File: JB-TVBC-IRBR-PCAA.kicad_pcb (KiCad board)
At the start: 2 copper layers, 20 x 25 mm, 7 parts, among them J1 SJ-435107, U1 TSOP75338WTT

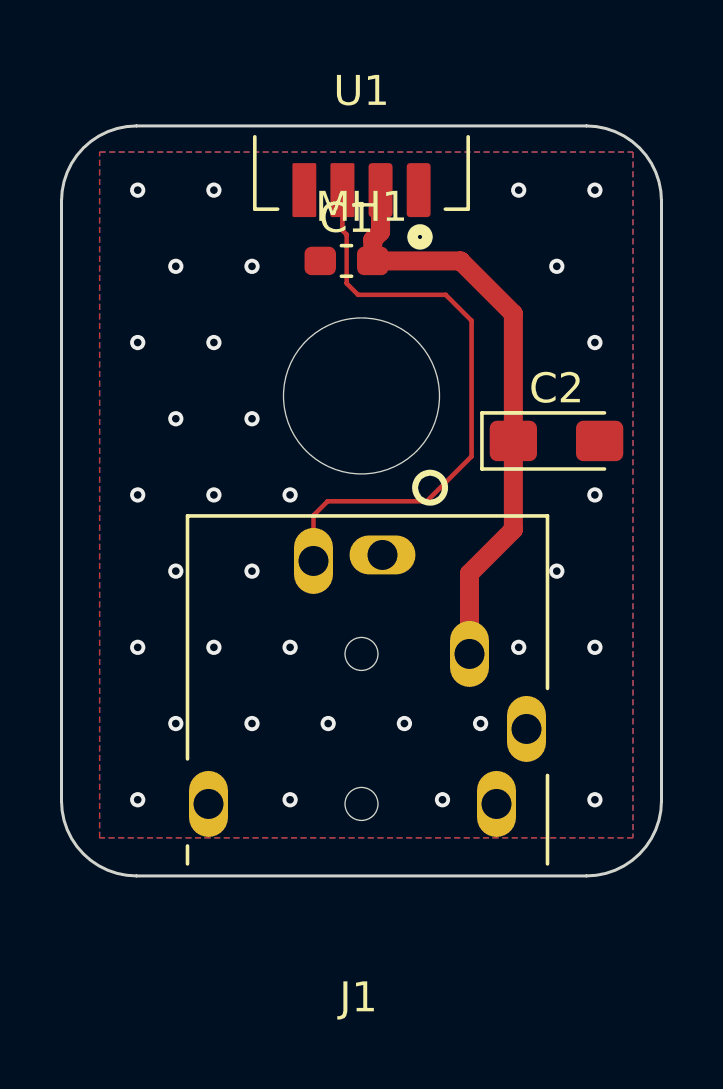
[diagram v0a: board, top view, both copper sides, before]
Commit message: clearing case + ref designator positioning
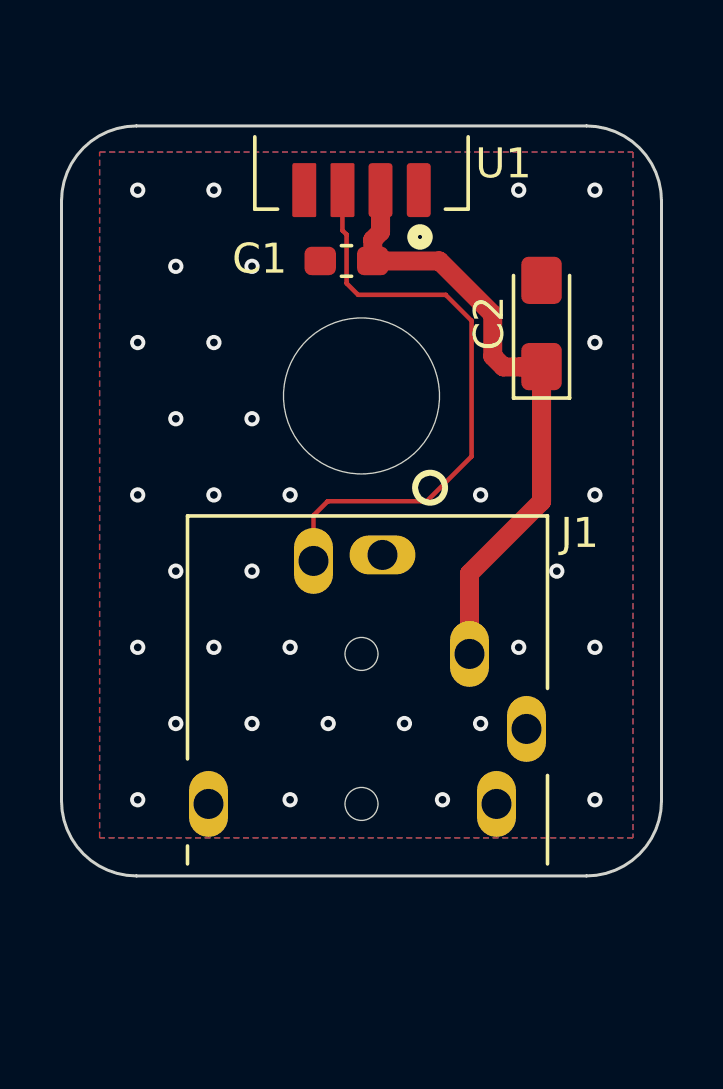
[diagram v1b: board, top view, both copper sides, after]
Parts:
- moved C2 3.95 mm to (156.0, 161.6), turned to 90 degrees
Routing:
- net +3V3: track 19.8 -> 21.0 mm
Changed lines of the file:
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@@
     (thickness 1.6)
     (drawings 11)
-    (tracks 53)
+    (tracks 57)
     (zones 0)
     (modules 7)
@@
   )
   (setup
-    (last_trace_width 0.1524)
+    (last_trace_width 0.635)
     (user_trace_width 0.1524)
     (user_trace_width 0.254)
@@
     (descr "TRS 3.5mm, horizontal, through-hole, with switch, circular holes, https://www.cui.com/product/resource/sj1-353xng.pdf")
     (tags "TRS audio jack stereo horizontal circular")
-    (fp_text reference J1 (at 0.1 -6.45 180) (layer F.SilkS)
+    (fp_text reference J1 (at -7.272 9.03 180) (layer F.SilkS)
       (effects (font (size 1 1) (thickness 0.15)))
     )
@@
     (tags "through hole")
     (attr virtual)
-    (fp_text reference MH1 (at 0 -6.3) (layer F.SilkS)
+    (fp_text reference MH1 (at 0 -6.3) (layer F.SilkS) hide
       (effects (font (size 1 1) (thickness 0.15)))
     )
@@
     (descr "TSOP753xx Right Angle")
     (tags "ir, ir receiver")
-    (fp_text reference U1 (at 0 2.413) (layer F.SilkS)
+    (fp_text reference U1 (at -4.732 -0.001) (layer F.SilkS)
       (effects (font (size 1 1) (thickness 0.15)))
     )
@@
   )
   (module Capacitor_Tantalum_SMD:CP_EIA-3216-18_Kemet-A_Pad1.58x1.35mm_HandSolder (layer F.Cu)
-    (at 156.5 165.5)
+    (at 156.002 161.585 90)
     (descr "Tantalum Capacitor SMD Kemet-A (3216-18 Metric), IPC_7351 nominal, (Body size from: http://www.kemet.com/Lists/ProductCatalog/Attachments/253/KEM_TC101_STD.pdf), generated with kicad-footprint-generator")
     (tags "capacitor tantalum")
     (attr smd)
-    (fp_text reference C2 (at 0 -1.75) (layer F.SilkS)
-      (effects (font (size 1 1) (thickness 0.15)))
-    )
-    (fp_text value 10UF_TANT_1206_16V (at 0 1.75) (layer F.Fab)
-      (effects (font (size 1 1) (thickness 0.15)))
-    )
-    (fp_text user %R (at 0 0) (layer F.Fab)
+    (fp_text reference C2 (at 0.01 -1.75 90) (layer F.SilkS)
+      (effects (font (size 1 1) (thickness 0.15)))
+    )
+    (fp_text value 10UF_TANT_1206_16V (at 0 1.75 90) (layer F.Fab)
+      (effects (font (size 1 1) (thickness 0.15)))
+    )
+    (fp_text user %R (at 0 0 90) (layer F.Fab)
       (effects (font (size 0.8 0.8) (thickness 0.12)))
     )
@@
     (fp_line (start -1.2 -0.8) (end -1.6 -0.4) (layer F.Fab) (width 0.1))
     (fp_line (start 1.6 -0.8) (end -1.2 -0.8) (layer F.Fab) (width 0.1))
-    (pad 2 smd roundrect (at 1.4375 0) (size 1.575 1.35) (layers F.Cu F.Paste F.Mask) (roundrect_rratio 0.185185)
+    (pad 2 smd roundrect (at 1.4375 0 90) (size 1.575 1.35) (layers F.Cu F.Paste F.Mask) (roundrect_rratio 0.185185)
       (net 2 GND))
-    (pad 1 smd roundrect (at -1.4375 0) (size 1.575 1.35) (layers F.Cu F.Paste F.Mask) (roundrect_rratio 0.185185)
+    (pad 1 smd roundrect (at -1.4375 0 90) (size 1.575 1.35) (layers F.Cu F.Paste F.Mask) (roundrect_rratio 0.185185)
       (net 1 +3V3))
     (model ${KISYS3DMOD}/Capacitor_Tantalum_SMD.3dshapes/CP_EIA-3216-18_Kemet-A.wrl
@@
     (tags "capacitor handsolder")
     (attr smd)
-    (fp_text reference C1 (at 0 -1.43) (layer F.SilkS)
+    (fp_text reference C1 (at -2.896 -0.074) (layer F.SilkS)
       (effects (font (size 1 1) (thickness 0.15)))
     )
@@
   (gr_line (start 142.5 180) (end 157.5 180) (layer Edge.Cuts) (width 0.1))
   (gr_line (start 140 157.5) (end 140 177.5) (layer Edge.Cuts) (width 0.1))
-  (segment (start 153.6 172.6) (end 153.6 169.9198) (width 0.635) (layer F.Cu) (net 1))
-  (segment (start 155.0625 168.4573) (end 155.0625 165.5) (width 0.635) (layer F.Cu) (net 1))
-  (segment (start 153.6 169.9198) (end 155.0625 168.4573) (width 0.635) (layer F.Cu) (net 1))
-  (segment (start 153.3024 159.5) (end 150.375 159.5) (width 0.635) (layer F.Cu) (net 1))
-  (segment (start 155.0625 161.2601) (end 153.3024 159.5) (width 0.635) (layer F.Cu) (net 1))
-  (segment (start 155.0625 165.5) (end 155.0625 161.2601) (width 0.635) (layer F.Cu) (net 1))
   (segment (start 150.375 159.5) (end 150.375 158.7938) (width 0.635) (layer F.Cu) (net 1))
   (segment (start 150.635 158.5338) (end 150.635 157.139) (width 0.635) (layer F.Cu) (net 1))
   (segment (start 150.375 158.7938) (end 150.635 158.5338) (width 0.635) (layer F.Cu) (net 1))
+  (segment (start 156.002 167.5178) (end 156.002 163.0225) (width 0.635) (layer F.Cu) (net 1))
+  (segment (start 153.6 172.6) (end 153.6 169.9198) (width 0.635) (layer F.Cu) (net 1))
+  (segment (start 153.6 169.9198) (end 156.002 167.5178) (width 0.635) (layer F.Cu) (net 1))
+  (segment (start 155.327 163.0225) (end 155.3167 163.0328) (width 0.635) (layer F.Cu) (net 1))
+  (segment (start 156.002 163.0225) (end 155.327 163.0225) (width 0.635) (layer F.Cu) (net 1))
+  (segment (start 155.3167 163.0328) (end 154.732 163.0328) (width 0.635) (layer F.Cu) (net 1))
+  (segment (start 154.732 163.0328) (end 154.3764 162.6772) (width 0.635) (layer F.Cu) (net 1))
+  (segment (start 154.3764 162.6772) (end 154.3764 161.2802) (width 0.635) (layer F.Cu) (net 1))
+  (segment (start 152.5962 159.5) (end 150.375 159.5) (width 0.635) (layer F.Cu) (net 1))
+  (segment (start 154.3764 161.2802) (end 152.5962 159.5) (width 0.635) (layer F.Cu) (net 1))
   (via (at 142.54 157.14) (size 0.508) (drill 0.254) (layers F.Cu B.Cu) (net 2))
   (via (at 155.24 157.14) (size 0.508) (drill 0.254) (layers F.Cu B.Cu) (net 2))
   (via (at 157.78 157.14) (size 0.508) (drill 0.254) (layers F.Cu B.Cu) (net 2))
-  (via (at 156.51 159.68) (size 0.508) (drill 0.254) (layers F.Cu B.Cu) (net 2))
   (via (at 146.35 159.68) (size 0.508) (drill 0.254) (layers F.Cu B.Cu) (net 2))
   (via (at 143.81 159.68) (size 0.508) (drill 0.254) (layers F.Cu B.Cu) (net 2))
@@
   (via (at 152.7 177.46) (size 0.508) (drill 0.254) (layers F.Cu B.Cu) (net 2))
   (via (at 157.78 177.46) (size 0.508) (drill 0.254) (layers F.Cu B.Cu) (net 2))
-  (via (at 145.08 157.14) (size 0.508) (drill 0.254) (layers F.Cu B.Cu) (net 2) (status 1000000))
+  (via (at 145.08 157.14) (size 0.508) (drill 0.254) (layers F.Cu B.Cu) (net 2))
+  (via (at 153.97 167.3) (size 0.508) (drill 0.254) (layers F.Cu B.Cu) (net 2))
   (segment (start 148.8694 167.513) (end 148.4 167.9824) (width 0.1524) (layer F.Cu) (net 5))
   (segment (start 148.4 167.9824) (end 148.4 169.5) (width 0.1524) (layer F.Cu) (net 5))
